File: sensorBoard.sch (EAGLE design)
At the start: 35 parts, among them Q1 BSS84, U1 ADXL345, U2 L3G4200D, U3 MPL115A, X1 22-23-2051

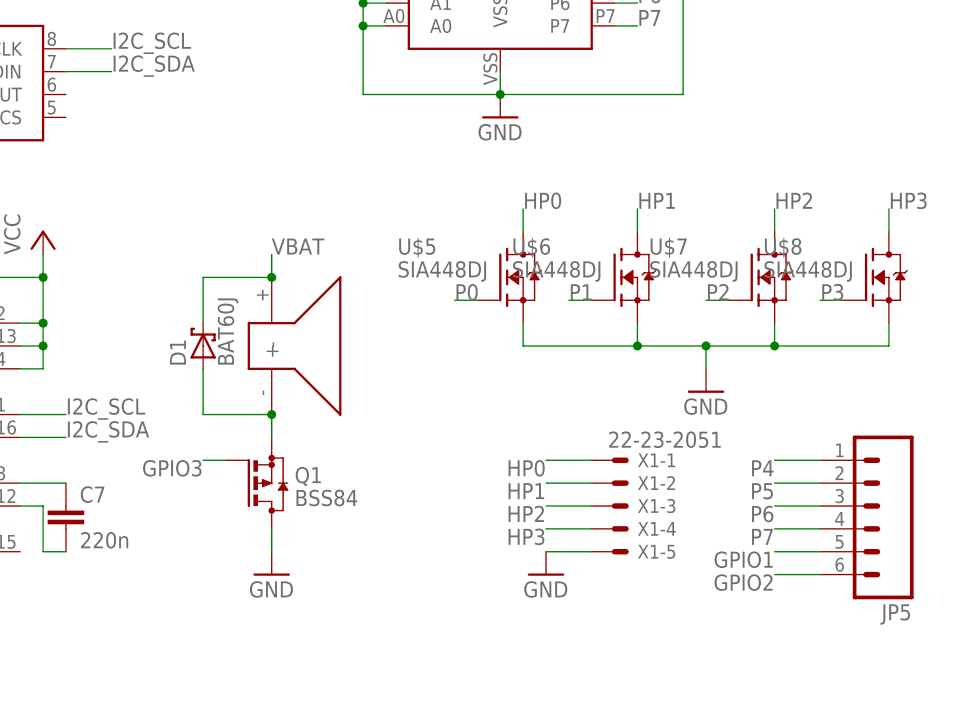
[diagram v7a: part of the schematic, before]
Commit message: Added pull-up resistors on mosfets
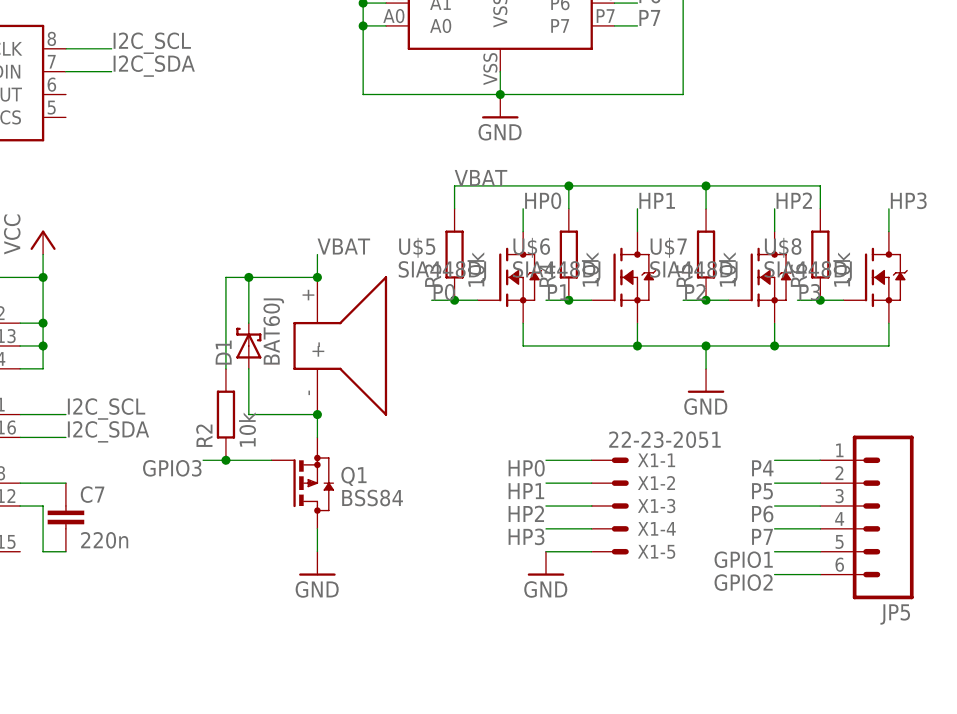
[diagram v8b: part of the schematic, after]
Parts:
- added R2, R3, R4, R5, R6: 10k, rcl:R-EU_R0402
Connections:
- net GPIO3: now also R2.1
- net P0: now also R3.1
- net P1: now also R4.1
- net P2: now also R5.1
- net P3: now also R6.1
- net VBAT: now also R2.2, R3.2, R4.2, R5.2, R6.2
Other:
- moved on the sheet: D1, Q1
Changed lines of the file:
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@@
 <part name="R1" library="rcl" deviceset="R-EU_" device="R0402" value="10k"/>
 <part name="U$10" library="earsLogo" deviceset="EARS-LOGO" device=""/>
+<part name="R2" library="rcl" deviceset="R-EU_" device="R0402" value="10k"/>
+<part name="R3" library="rcl" deviceset="R-EU_" device="R0402" value="10k"/>
+<part name="R4" library="rcl" deviceset="R-EU_" device="R0402" value="10k"/>
+<part name="R5" library="rcl" deviceset="R-EU_" device="R0402" value="10k"/>
+<part name="R6" library="rcl" deviceset="R-EU_" device="R0402" value="10k"/>
 </parts>
 <sheets>
@@
 <instance part="P+6" gate="VCC" x="142.24" y="81.28"/>
 <instance part="GND7" gate="1" x="139.7" y="58.42"/>
-<instance part="U$3" gate="G$1" x="193.04" y="38.1">
-<attribute name="OC_FARNELL" x="193.04" y="38.1" size="1.778" layer="96" display="off"/>
+<instance part="U$3" gate="G$1" x="198.12" y="38.1">
+<attribute name="OC_FARNELL" x="198.12" y="38.1" size="1.778" layer="96" display="off"/>
 </instance>
-<instance part="Q1" gate="G$1" x="193.04" y="22.86"/>
-<instance part="GND8" gate="1" x="193.04" y="12.7"/>
+<instance part="Q1" gate="G$1" x="198.12" y="22.86"/>
+<instance part="GND8" gate="1" x="198.12" y="12.7"/>
 <instance part="U$4" gate="G$1" x="218.44" y="78.74"/>
 <instance part="P+7" gate="VCC" x="218.44" y="104.14"/>
@@
 <instance part="L1" gate="G$1" x="17.78" y="101.6" rot="R180"/>
 <instance part="C12" gate="G$1" x="137.16" y="66.04"/>
-<instance part="D1" gate="G$1" x="185.42" y="38.1" rot="R90">
-<attribute name="OC_FARNELL" x="185.42" y="38.1" size="1.778" layer="96" rot="R90" display="off"/>
+<instance part="D1" gate="G$1" x="190.5" y="38.1" rot="R90">
+<attribute name="OC_FARNELL" x="190.5" y="38.1" size="1.778" layer="96" rot="R90" display="off"/>
 </instance>
 <instance part="GND11" gate="1" x="127" y="78.74"/>
@@
 <instance part="R1" gate="G$1" x="119.38" y="12.7" rot="R90"/>
 <instance part="U$10" gate="G$1" x="2.54" y="0"/>
+<instance part="R2" gate="G$1" x="187.96" y="30.48" rot="R90"/>
+<instance part="R3" gate="G$1" x="213.36" y="48.26" rot="R90"/>
+<instance part="R4" gate="G$1" x="226.06" y="48.26" rot="R90"/>
+<instance part="R5" gate="G$1" x="241.3" y="48.26" rot="R90"/>
+<instance part="R6" gate="G$1" x="254" y="48.26" rot="R90"/>
 </instances>
 <busses>
@@
 <pinref part="Q1" gate="G$1" pin="D"/>
 <pinref part="GND8" gate="1" pin="GND"/>
-<wire x1="193.04" y1="15.24" x2="193.04" y2="17.78" width="0.1524" layer="91"/>
+<wire x1="198.12" y1="15.24" x2="198.12" y2="17.78" width="0.1524" layer="91"/>
 </segment>
 <segment>
@@
 <segment>
 <pinref part="U$3" gate="G$1" pin="+"/>
-<wire x1="193.04" y1="45.72" x2="193.04" y2="48.26" width="0.1524" layer="91"/>
-<label x="193.04" y="48.26" size="1.778" layer="95"/>
+<wire x1="198.12" y1="45.72" x2="198.12" y2="48.26" width="0.1524" layer="91"/>
+<label x="198.12" y="48.26" size="1.778" layer="95"/>
 <pinref part="D1" gate="G$1" pin="C"/>
-<wire x1="185.42" y1="40.64" x2="185.42" y2="45.72" width="0.1524" layer="91"/>
-<wire x1="185.42" y1="45.72" x2="193.04" y2="45.72" width="0.1524" layer="91"/>
-<junction x="193.04" y="45.72"/>
+<wire x1="190.5" y1="40.64" x2="190.5" y2="45.72" width="0.1524" layer="91"/>
+<wire x1="190.5" y1="45.72" x2="198.12" y2="45.72" width="0.1524" layer="91"/>
+<junction x="198.12" y="45.72"/>
+<pinref part="R2" gate="G$1" pin="2"/>
+<wire x1="187.96" y1="35.56" x2="187.96" y2="45.72" width="0.1524" layer="91"/>
+<wire x1="187.96" y1="45.72" x2="190.5" y2="45.72" width="0.1524" layer="91"/>
+<junction x="190.5" y="45.72"/>
+</segment>
+<segment>
+<pinref part="R3" gate="G$1" pin="2"/>
+<wire x1="213.36" y1="53.34" x2="213.36" y2="55.88" width="0.1524" layer="91"/>
+<pinref part="R6" gate="G$1" pin="2"/>
+<wire x1="213.36" y1="55.88" x2="226.06" y2="55.88" width="0.1524" layer="91"/>
+<wire x1="226.06" y1="55.88" x2="241.3" y2="55.88" width="0.1524" layer="91"/>
+<wire x1="241.3" y1="55.88" x2="254" y2="55.88" width="0.1524" layer="91"/>
+<wire x1="254" y1="55.88" x2="254" y2="53.34" width="0.1524" layer="91"/>
+<pinref part="R5" gate="G$1" pin="2"/>
+<wire x1="241.3" y1="53.34" x2="241.3" y2="55.88" width="0.1524" layer="91"/>
+<junction x="241.3" y="55.88"/>
+<pinref part="R4" gate="G$1" pin="2"/>
+<wire x1="226.06" y1="53.34" x2="226.06" y2="55.88" width="0.1524" layer="91"/>
+<junction x="226.06" y="55.88"/>
+<label x="213.36" y="55.88" size="1.778" layer="95"/>
 </segment>
 </net>
@@
 <segment>
 <pinref part="Q1" gate="G$1" pin="G"/>
+<wire x1="193.04" y1="25.4" x2="187.96" y2="25.4" width="0.1524" layer="91"/>
+<label x="185.42" y="25.4" size="1.778" layer="95" rot="R180"/>
+<pinref part="R2" gate="G$1" pin="1"/>
 <wire x1="187.96" y1="25.4" x2="185.42" y2="25.4" width="0.1524" layer="91"/>
-<label x="185.42" y="25.4" size="1.778" layer="95" rot="R180"/>
+<junction x="187.96" y="25.4"/>
 </segment>
 </net>
@@
 <pinref part="U$3" gate="G$1" pin="-"/>
 <pinref part="Q1" gate="G$1" pin="S"/>
-<wire x1="193.04" y1="27.94" x2="193.04" y2="30.48" width="0.1524" layer="91"/>
+<wire x1="198.12" y1="27.94" x2="198.12" y2="30.48" width="0.1524" layer="91"/>
 <pinref part="D1" gate="G$1" pin="A"/>
-<wire x1="185.42" y1="35.56" x2="185.42" y2="30.48" width="0.1524" layer="91"/>
-<wire x1="185.42" y1="30.48" x2="193.04" y2="30.48" width="0.1524" layer="91"/>
-<junction x="193.04" y="30.48"/>
+<wire x1="190.5" y1="35.56" x2="190.5" y2="30.48" width="0.1524" layer="91"/>
+<wire x1="190.5" y1="30.48" x2="198.12" y2="30.48" width="0.1524" layer="91"/>
+<junction x="198.12" y="30.48"/>
 </segment>
 </net>
@@
 <pinref part="U$5" gate="G$1" pin="G"/>
 <wire x1="215.9" y1="43.18" x2="213.36" y2="43.18" width="0.1524" layer="91"/>
-<label x="213.36" y="43.18" size="1.778" layer="95"/>
+<label x="210.82" y="43.18" size="1.778" layer="95"/>
+<pinref part="R3" gate="G$1" pin="1"/>
+<wire x1="213.36" y1="43.18" x2="210.82" y2="43.18" width="0.1524" layer="91"/>
+<junction x="213.36" y="43.18"/>
 </segment>
 <segment>
@@
 <pinref part="U$6" gate="G$1" pin="G"/>
 <wire x1="228.6" y1="43.18" x2="226.06" y2="43.18" width="0.1524" layer="91"/>
-<label x="226.06" y="43.18" size="1.778" layer="95"/>
+<label x="223.52" y="43.18" size="1.778" layer="95"/>
+<pinref part="R4" gate="G$1" pin="1"/>
+<wire x1="226.06" y1="43.18" x2="223.52" y2="43.18" width="0.1524" layer="91"/>
+<junction x="226.06" y="43.18"/>
 </segment>
 <segment>
@@
 <pinref part="U$7" gate="G$1" pin="G"/>
 <wire x1="243.84" y1="43.18" x2="241.3" y2="43.18" width="0.1524" layer="91"/>
-<label x="241.3" y="43.18" size="1.778" layer="95"/>
+<label x="238.76" y="43.18" size="1.778" layer="95"/>
+<pinref part="R5" gate="G$1" pin="1"/>
+<wire x1="241.3" y1="43.18" x2="238.76" y2="43.18" width="0.1524" layer="91"/>
+<junction x="241.3" y="43.18"/>
 </segment>
 <segment>
@@
 <pinref part="U$8" gate="G$1" pin="G"/>
 <wire x1="256.54" y1="43.18" x2="254" y2="43.18" width="0.1524" layer="91"/>
-<label x="254" y="43.18" size="1.778" layer="95"/>
-</segment>
-<segment>
+<label x="251.46" y="43.18" size="1.778" layer="95"/>
+<pinref part="R6" gate="G$1" pin="1"/>
+<wire x1="254" y1="43.18" x2="251.46" y2="43.18" width="0.1524" layer="91"/>
+<junction x="254" y="43.18"/>
+</segment>
+<segment>
